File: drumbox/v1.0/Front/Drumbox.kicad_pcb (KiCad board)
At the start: 2 copper layers, 120 x 128 mm, 4 parts

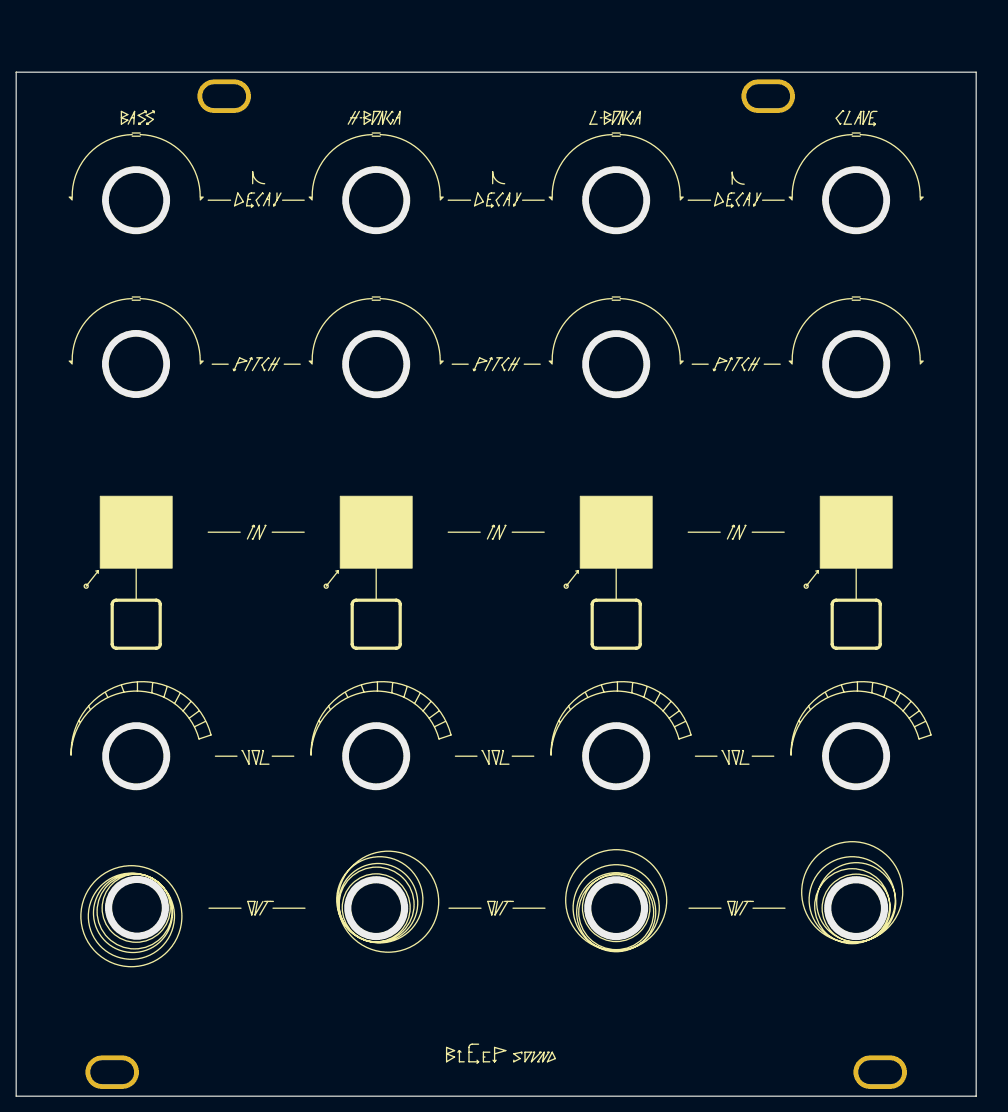
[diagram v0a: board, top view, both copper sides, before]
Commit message: fixed size issues on front panel drumbox
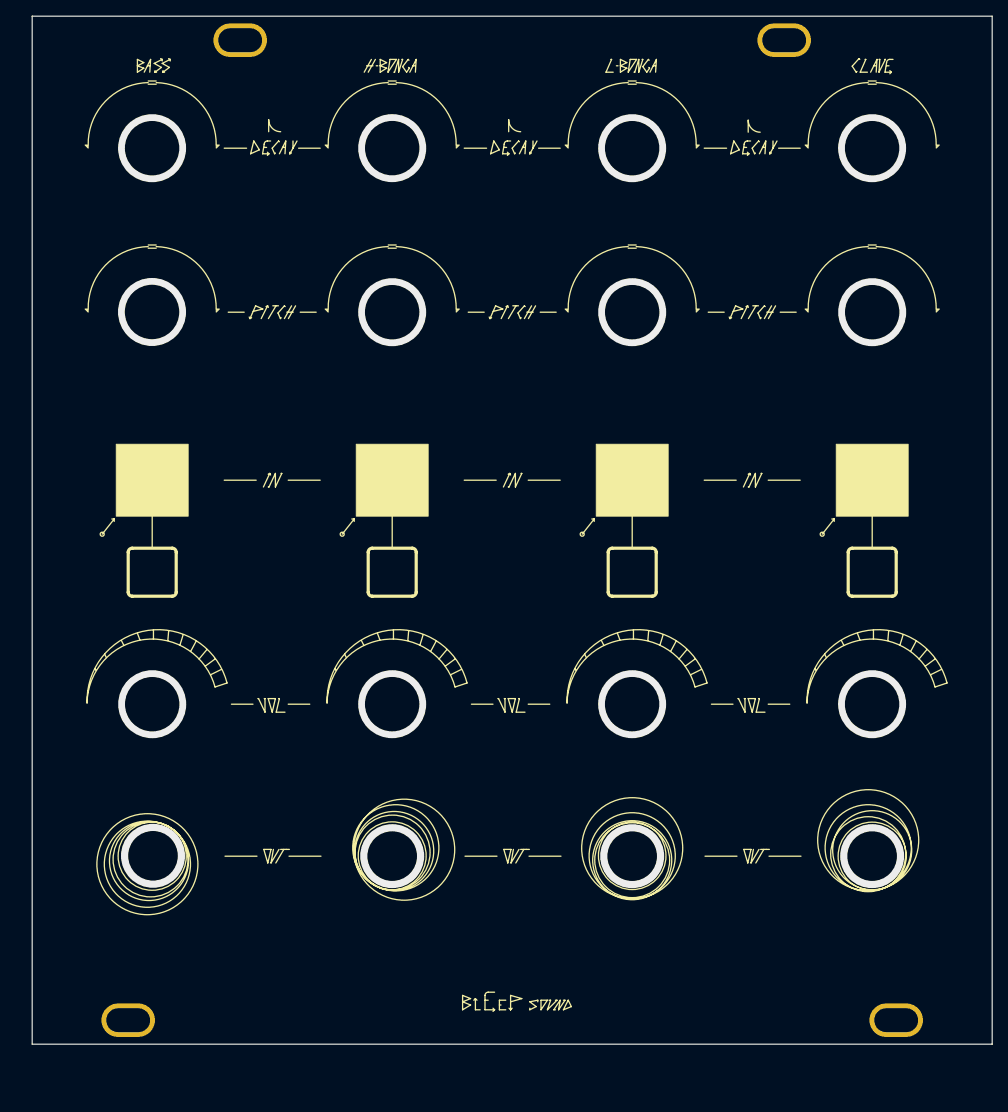
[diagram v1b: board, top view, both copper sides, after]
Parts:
- removed the ? at (52.0, 168.5)
- removed the ? at (148.0, 168.5)
- removed REF** (x2): Doepfer Mounting hole, Synth:Doepfer Mounting hole
- added ?: , , F.Cu at (54.0, 162.0)
- added ?: , , F.Cu at (136.0, 39.5)
- added ?: , , F.Cu at (68.0, 39.5)
- added ?: , , F.Cu at (150.0, 162.0)
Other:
- board size 120 x 128 mm -> 120 x 128.5 mm
